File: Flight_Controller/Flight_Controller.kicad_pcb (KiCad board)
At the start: 2 copper layers, 68 parts, among them IC1 AT7456E, J1 XT30, J10 USB_C_Receptacle_USB2.0_16P, J11 Conn_ARM_SWD_TagConnect_TC203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, J13 SM06B-GHS-TB, J14 VTX, J6 ESC->FC DSHOT and Telem, J7 ELRS Reciever, J9 Camera, SW1 SW_Push, U1 STM32H743VITx, U2 BMI270, U3 TLV75533PDBV, U4 W25Q128JVSIQ TR, U5 TPS62932, U7 TPD2EUSB30ADRTR, Y2 ABM3-27.000MHZ-D2Y-T

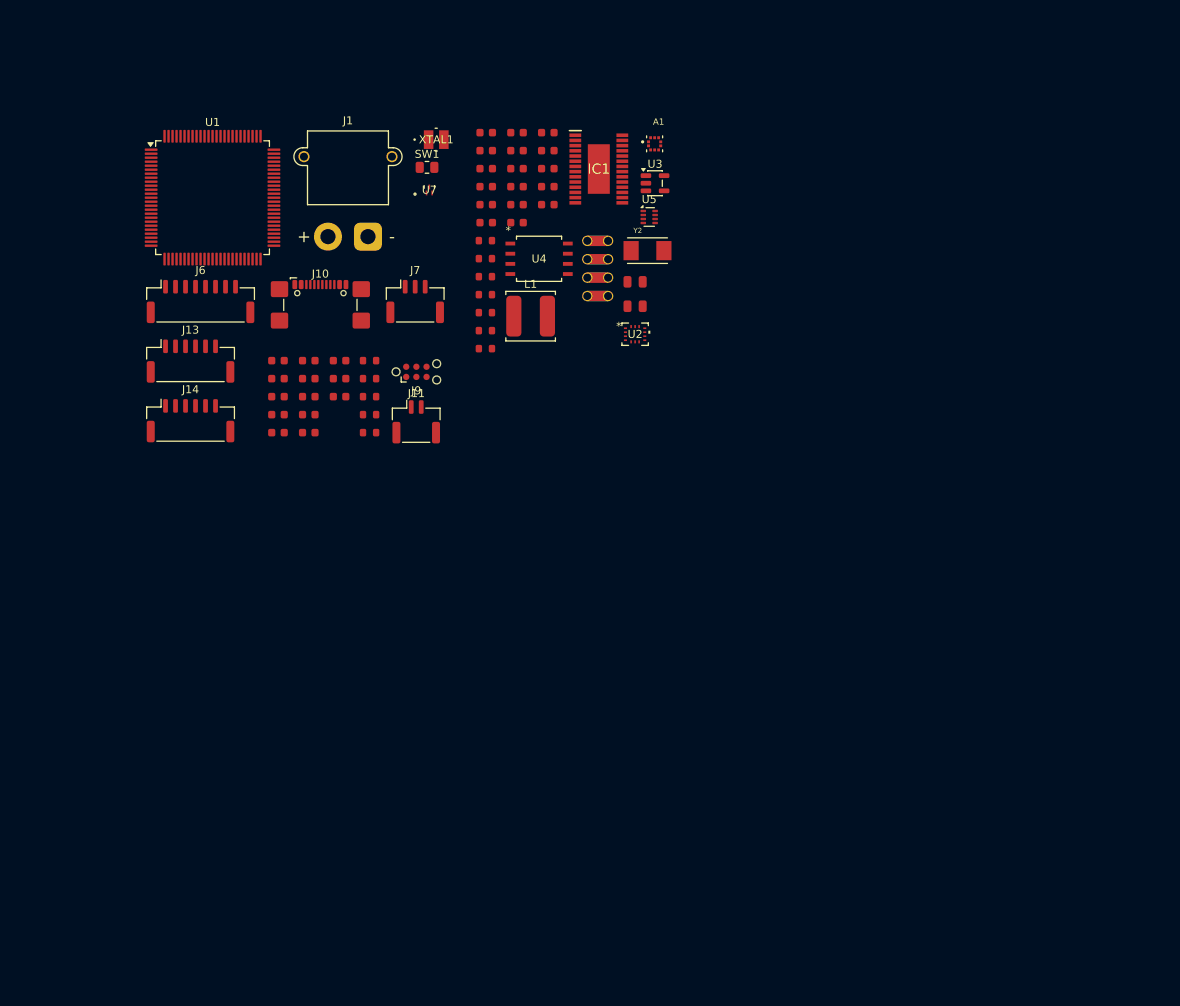
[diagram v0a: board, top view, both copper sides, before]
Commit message: PCB clustering
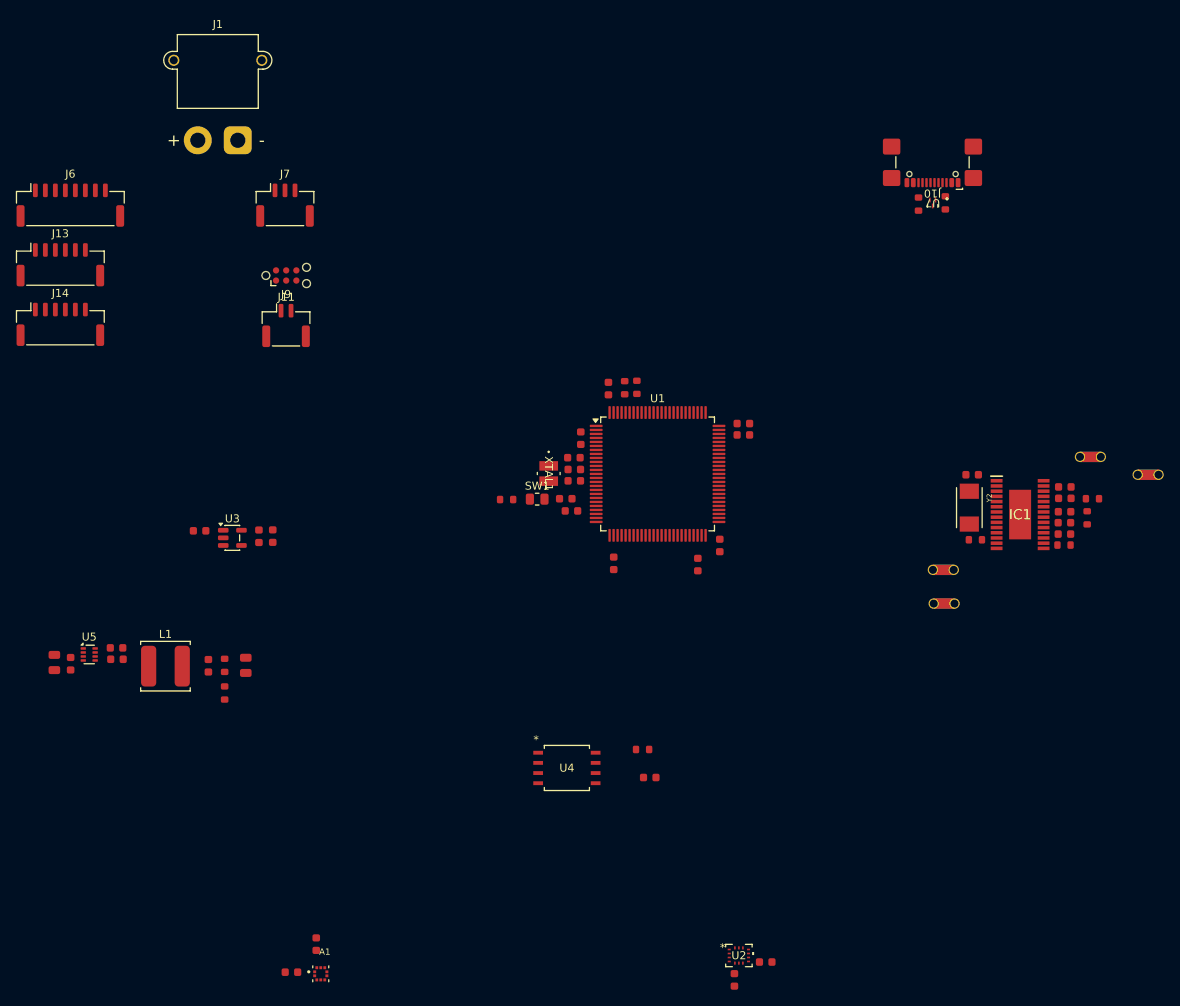
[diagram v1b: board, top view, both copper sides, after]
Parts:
- moved A1 111.8 mm to (55.6, 128.4)
- moved C9 106.5 mm to (52.0, 128.2), turned to 180 degrees
- moved C24 105.0 mm to (111.3, 126.9)
- moved C8 104.5 mm to (55.1, 124.7), turned to 90 degrees
- moved C6 101.8 mm to (107.3, 129.1), turned to -90 degrees
- moved U5 88.8 mm to (26.7, 88.5)
- moved C1 86.4 mm to (148.6, 70.6)
- moved C33 85.2 mm to (22.3, 89.5), turned to -90 degrees
- moved C2 83.7 mm to (148.6, 67.5)
- moved C3 83.2 mm to (148.6, 68.9)
- moved R1 81.7 mm to (148.5, 74.8), turned to 180 degrees
- moved R4 81.0 mm to (151.4, 71.4), turned to -90 degrees
- moved R5 80.1 mm to (152.1, 69.0)
- moved J10 79.1 mm to (132.1, 25.8), turned to 180 degrees
- moved U2 78.7 mm to (107.9, 126.1)
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
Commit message: Rough Layout + LEDs
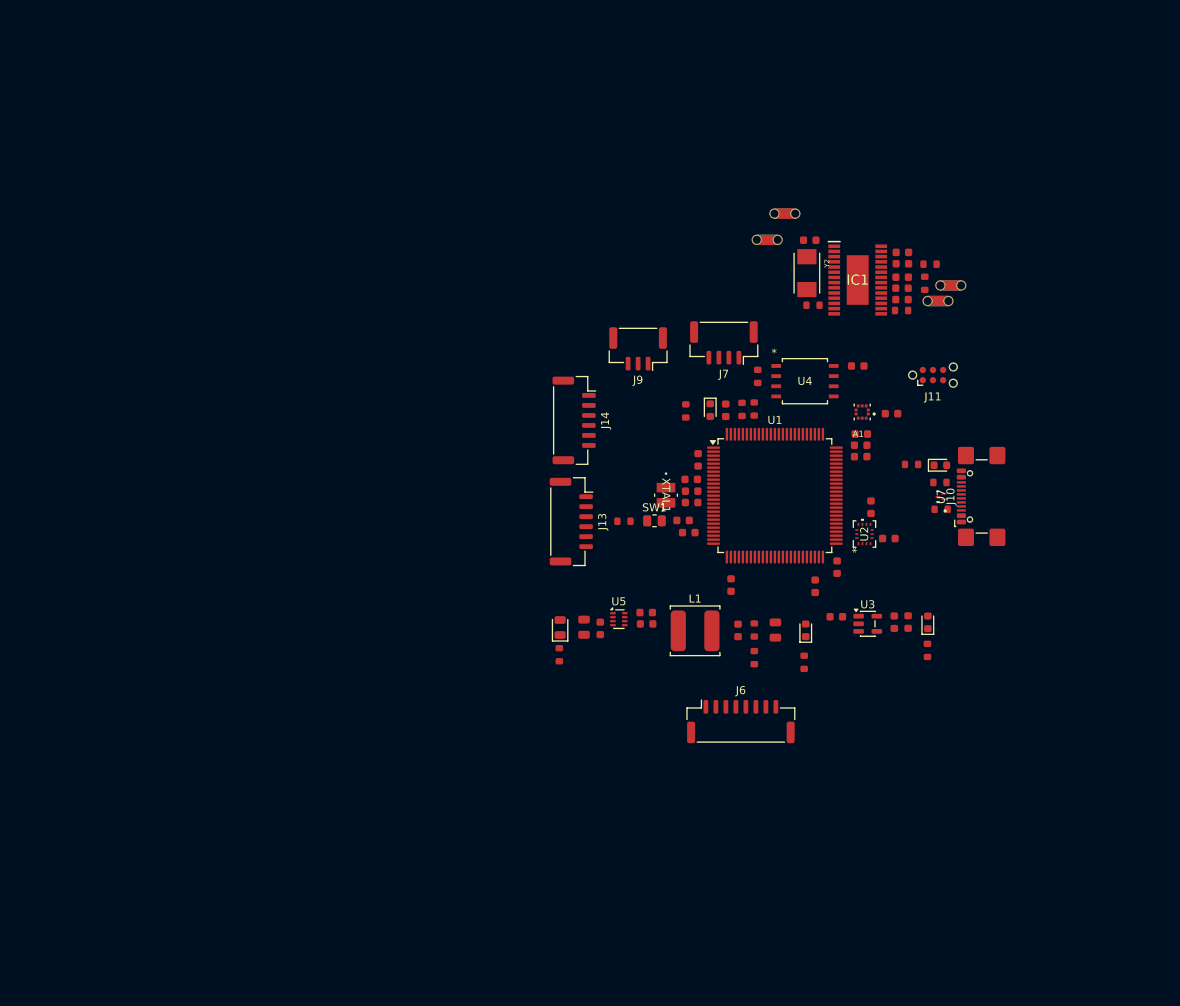
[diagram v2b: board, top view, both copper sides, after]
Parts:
- removed J1: XT30, Connector_AMASS:AMASS_XT30PW-M_1x02_P2.50mm_Horizontal
- added D1: Red, PCM_JLCPCB:D_0603, F.Cu at (104.3, 57.9)
- added D2: White, PCM_JLCPCB:D_0603, F.Cu at (133.1, 64.8)
- added D3: White, PCM_JLCPCB:D_0603, F.Cu at (116.3, 85.4)
- added D4: Green, PCM_JLCPCB:D_0805, F.Cu at (85.6, 85.1)
- added D5: Red, PCM_JLCPCB:D_0603, F.Cu at (131.5, 84.4)
- added R10: 430Ω, PCM_JLCPCB:R_0603, F.Cu at (129.5, 64.7)
- added R15: 430Ω, PCM_JLCPCB:R_0603, F.Cu at (116.1, 89.4)
- added R16: 2.7kΩ, PCM_JLCPCB:R_0603, F.Cu at (85.5, 88.5)
- added R17: 150Ω, PCM_JLCPCB:R_0603, F.Cu at (131.5, 87.9)
- added R9: 150Ω, PCM_JLCPCB:R_0603, F.Cu at (101.3, 58.0)
- J7: footprint Connector_JST:JST_GH_SM03B-GHS-TB_1x03-1MP_P1.25mm_Horizontal -> Connector_JST:JST_GH_SM04B-GHS-TB_1x04-1MP_P1.25mm_Horizontal
- J9: footprint Connector_JST:JST_GH_SM02B-GHS-TB_1x02-1MP_P1.25mm_Horizontal -> Connector_JST:JST_GH_SM03B-GHS-TB_1x03-1MP_P1.25mm_Horizontal
- moved J6 105.8 mm to (108.2, 96.8)
- moved C9 102.5 mm to (127.0, 58.4), turned to 0 degrees
- moved A1 97.5 mm to (123.3, 58.1), turned to 180 degrees
- moved C8 93.3 mm to (123.2, 60.9), turned to 0 degrees
- moved J11 81.8 mm to (132.2, 53.5)
- moved C14 80.3 mm to (120.1, 83.7)
- moved C15 80.1 mm to (127.3, 84.4)
- moved C17 80.1 mm to (129.1, 84.4)
- moved U3 80.1 mm to (124.0, 84.6)
- moved J13 71.5 mm to (87.0, 71.8), turned to -90 degrees
- moved C10 66.4 mm to (96.3, 83.2)
- moved C11 66.4 mm to (96.4, 84.6)
- moved C12 66.4 mm to (107.8, 85.4)
- moved C13 66.4 mm to (112.5, 85.4)
- moved C33 66.4 mm to (88.5, 85.0)
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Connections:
- net /MCU/Connectors/SPI_CLK renamed /MCU/Connectors/SPI_SCK
- net /MCU/Connectors/VIDEO_IN renamed /Peripherals/Power/<NO NET>
- net Net-(C2-Pad2) renamed /Peripherals/Power/VOUT_RES
- net Net-(C28-Pad1) renamed /MCU/Connectors/VCAP2
- net Net-(C29-Pad1) renamed /MCU/Connectors/VCAP1
- net Net-(IC1-SAG) renamed /Peripherals/Power/OSD_SAG
- net Net-(IC1-VIN) renamed /Peripherals/Power/OSD_VIN
- net Net-(IC1-VOUT) renamed /Peripherals/Power/OSD_VOUT
- net Net-(R14-Pad2) renamed /MCU/Connectors/RST_SW
- net Net-(U5-SS) renamed /Peripherals/Power/SS
- J6 pad 7: GND -> +BATT
- U1 pad 77: /MCU/Connectors/OSD_SPI_CS -> unconnected-(U1-PA15-Pad77)
- U1 pad 85: unconnected-(U1-PD4-Pad85) -> /MCU/Connectors/OSD_SPI_CS
- U2 pad 12: /MCU/Connectors/IMU_INT -> /MCU/Connectors/IMU_SPI_CS
- U2 pad 4: /MCU/Connectors/IMU_SPI_CS -> /MCU/Connectors/IMU_INT
